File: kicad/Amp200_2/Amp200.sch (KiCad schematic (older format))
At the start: 38 parts, among them J1 Conn, J10 Conn, J2 Conn, J3 Conn, J5 Conn, J6 Conn, J7 Conn, J8 Conn, J9 Conn, U2 NCP1117-3.3

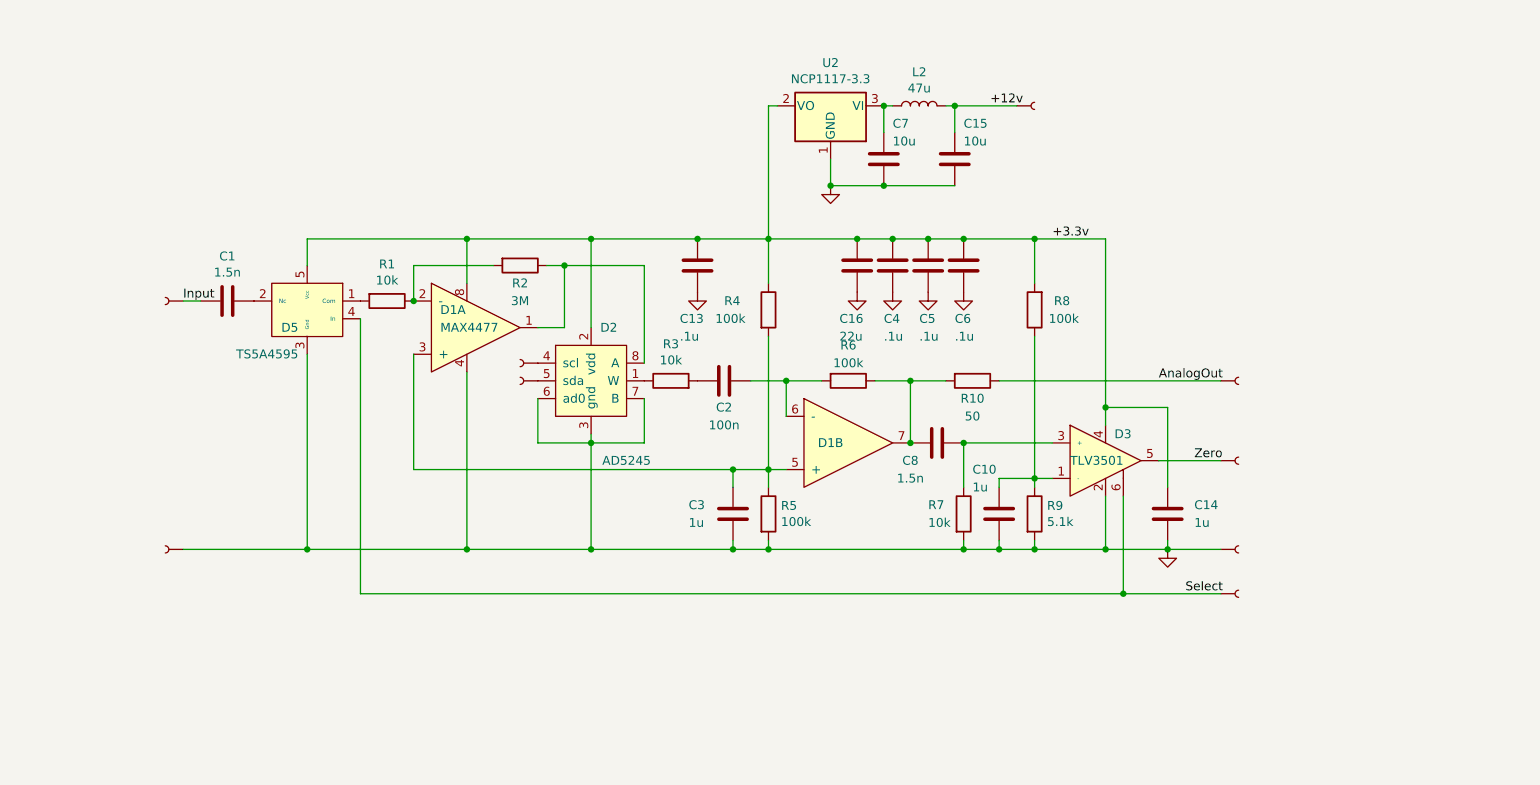
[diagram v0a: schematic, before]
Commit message: изменено:      kicad/Amp200_2/Amp200-cache.lib 	изменено:      kicad/Amp200_2/Amp200.kicad_pcb 	изменено:      kicad/Amp200_2/Amp200.kicad_pcb-bak 	изменено:      kicad/Amp200_2/Amp200.sch 	изменено:      kicad/Amp200_2/Amp200.sch-bak 	изменено:      kicad/Amp200_2/fp-info-cache 	изменено:      kicad/Anemometr_200_F303/fp-info-cache 	изменено:      stm32cubeide/Anemometer/Release/makefile 	изменено:      stm32cubeide/Anemometer_200_F303/Anemometer_200_F303.ioc 	изменено:      stm32cubeide/Anemometer_200_F303/Core/Inc/main.h 	изменено:      stm32cubeide/Anemometer_200_F303/Core/Inc/stm32f3xx_it.h 	изменено:      stm32cubeide/Anemometer_200_F303/Core/Src/main.c 	изменено:      stm32cubeide/Anemometer_200_F303/Core/Src/stm32f3xx_hal_msp.c 	изменено:      stm32cubeide/Anemometer_200_F303/Core/Src/stm32f3xx_it.c 	изменено:      stm32cubeide/Anemometer_200_F303/Debug/Anemometer_200_F303.bin 	изменено:      stm32cubeide/Anemometer_200_F303/Debug/Anemometer_200_F303.elf 	изменено:      stm32cubeide/Anemometer_200_F303/Debug/Anemometer_200_F303.list 	изменено:      stm32cubeide/Anemometer_200_F303/Debug/Anemometer_200_F303.map 	изменено:      stm32cubeide/Anemometer_200_F303/Debug/Core/Src/main.o 	изменено:      stm32cubeide/Anemometer_200_F303/Debug/Core/Src/main.su 	изменено:      stm32cubeide/Anemometer_200_F303/Debug/Core/Src/stm32f3xx_hal_msp.o 	изменено:      stm32cubeide/Anemometer_200_F303/Debug/Core/Src/stm32f3xx_hal_msp.su 	изменено:      stm32cubeide/Anemometer_200_F303/Debug/Core/Src/stm32f3xx_it.o 	изменено:      stm32cubeide/Anemometer_200_F303/Debug/Core/Src/stm32f3xx_it.su
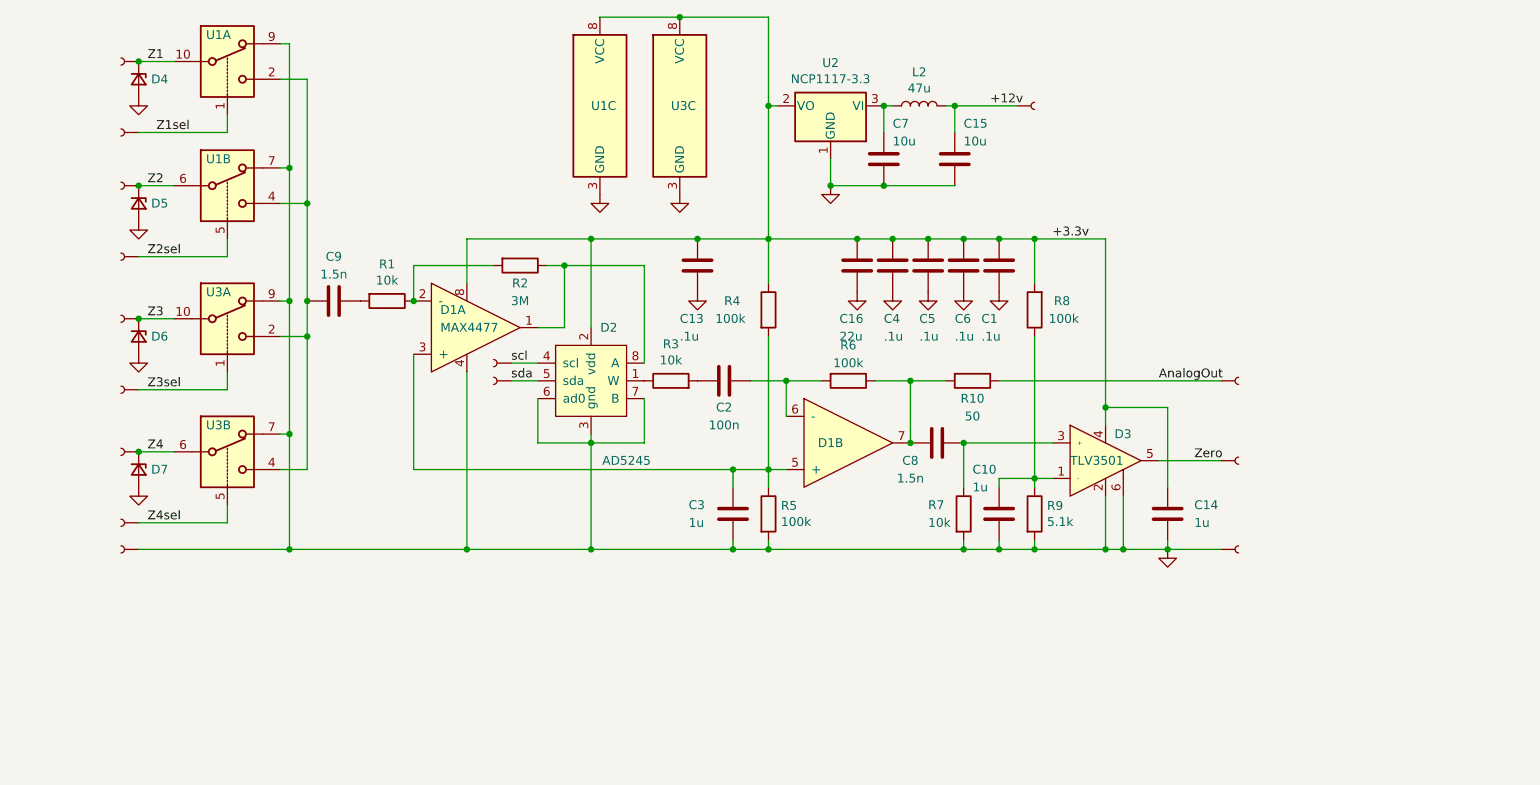
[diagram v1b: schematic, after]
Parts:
- removed D5: TS5A4595, Package_TO_SOT_SMD:SOT-23-5, symbol Amp200-rescue:TS5A4595-My_Library
- added C9: 1.5n, Capacitor_SMD:C_0603_1608Metric, symbol Device:C
- added D4, D5, D6, D7: BZ55C2V7, Diode_SMD:D_MiniMELF, symbol Device:D_Zener_Small
- added J11, J12, J13, J14, J15, J16: Conn, My-library:SMD-CONN, symbol Amp200-rescue:Conn-My_Library
- added U1, U3: TS5A23159DGS, Package_SO:VSSOP-10_3x3mm_P0.5mm, symbol Analog_Switch:TS5A23159DGS
- C1: value 1.5n -> .1u; footprint Capacitor_SMD:C_0603_1608Metric -> Capacitor_SMD:C_0805_2012Metric
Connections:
- net +3.3v: now also C1.1, U1.8 (VCC), U3.8 (VCC)
- net GND: now also C1.2, D3.6, D4.2 (A), D5.2 (A), D6.2 (A), D7.2 (A), U1.3 (GND), U1.7, U1.9, U3.3 (GND), U3.7, U3.9
- net at R1.2: now also C9.1
- net scl: now reaches D2.4 (scl), J2.1
- net sda: now reaches D2.5 (sda), J3.1
- net Input renamed Z1
- net Z1: now also D4.1 (K), U1.10; no longer C1.2
- net Select renamed Z1sel
- net Z1sel: now also U1.1; no longer D3.6
- new net: C9.2, U1.2, U1.4, U3.2, U3.4
- new net Z2: D5.1 (K), J11.1, U1.6
- new net Z2sel: J12.1, U1.5
- new net Z3: D6.1 (K), J13.1, U3.10
- new net Z3sel: J14.1, U3.1
- new net Z4: D7.1 (K), J15.1, U3.6
- new net Z4sel: J16.1, U3.5

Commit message: изменено:      kicad/Amp200_2/Amp200-cache.lib 	изменено:      kicad/Amp200_2/Amp200.kicad_pcb 	изменено:      kicad/Amp200_2/Amp200.kicad_pcb-bak 	изменено:      kicad/Amp200_2/Amp200.sch 	изменено:      kicad/Amp200_2/Amp200.sch-bak 	изменено:      kicad/Amp200_2/fp-info-cache 	изменено:      kicad/Anemometr_200_F303/Anemometr_200_F303.kicad_pcb 	изменено:      kicad/Anemometr_200_F303/Anemometr_200_F303.kicad_pcb-bak 	изменено:      kicad/Anemometr_200_F303/Anemometr_200_F303.sch 	изменено:      kicad/Anemometr_200_F303/Anemometr_200_F303.sch-bak 	изменено:      stm32cubeide/Anemometer_200_F303/.cproject 	изменено:      stm32cubeide/Anemometer_200_F303/.mxproject 	изменено:      stm32cubeide/Anemometer_200_F303/.settings/language.settings.xml 	изменено:      stm32cubeide/Anemometer_200_F303/.settings/stm32cubeide.project.prefs 	изменено:      stm32cubeide/Anemometer_200_F303/Anemometer_200_F303.ioc 	изменено:      stm32cubeide/Anemometer_200_F303/Anemometer_200_F303.launch 	изменено:      stm32cubeide/Anemometer_200_F303/Core/Inc/main.h 	изменено:      stm32cubeide/Anemometer_200_F303/Core/Inc/stm32f3xx_hal_conf.h 	изменено:      stm32cubeide/Anemometer_200_F303/Core/Inc/stm32f3xx_it.h 	изменено:      stm32cubeide/Anemometer_200_F303/Core/Src/main.c 	изменено:      stm32cubeide/Anemometer_200_F303/Core/Src/stm32f3xx_hal_msp.c 	изменено:      stm32cubeide/Anemometer_200_F303/Core/Src/stm32f3xx_it.c 	удалено:       stm32cubeide/Anemometer_200_F303/Debug/Anemometer_200_F303.bin 	изменено:      stm32cubeide/Anemometer_200_F303/Debug/Anemometer_200_F303.elf 	изменено:      stm32cubeide/Anemometer_200_F303/Debug/Anemometer_200_F303.list 	изменено:      stm32cubeide/Anemometer_200_F303/Debug/Anemometer_200_F303.map 	изменено:      stm32cubeide/Anemometer_200_F303/Debug/Core/Src/main.d 	изменено:      stm32cubeide/Anemometer_200_F303/Debug/Core/Src/main.o 	изменено:      stm32cubeide/Anemometer_200_F303/Debug/Core/Src/main.su 	изменено:      stm32cubeide/Anemometer_200_F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
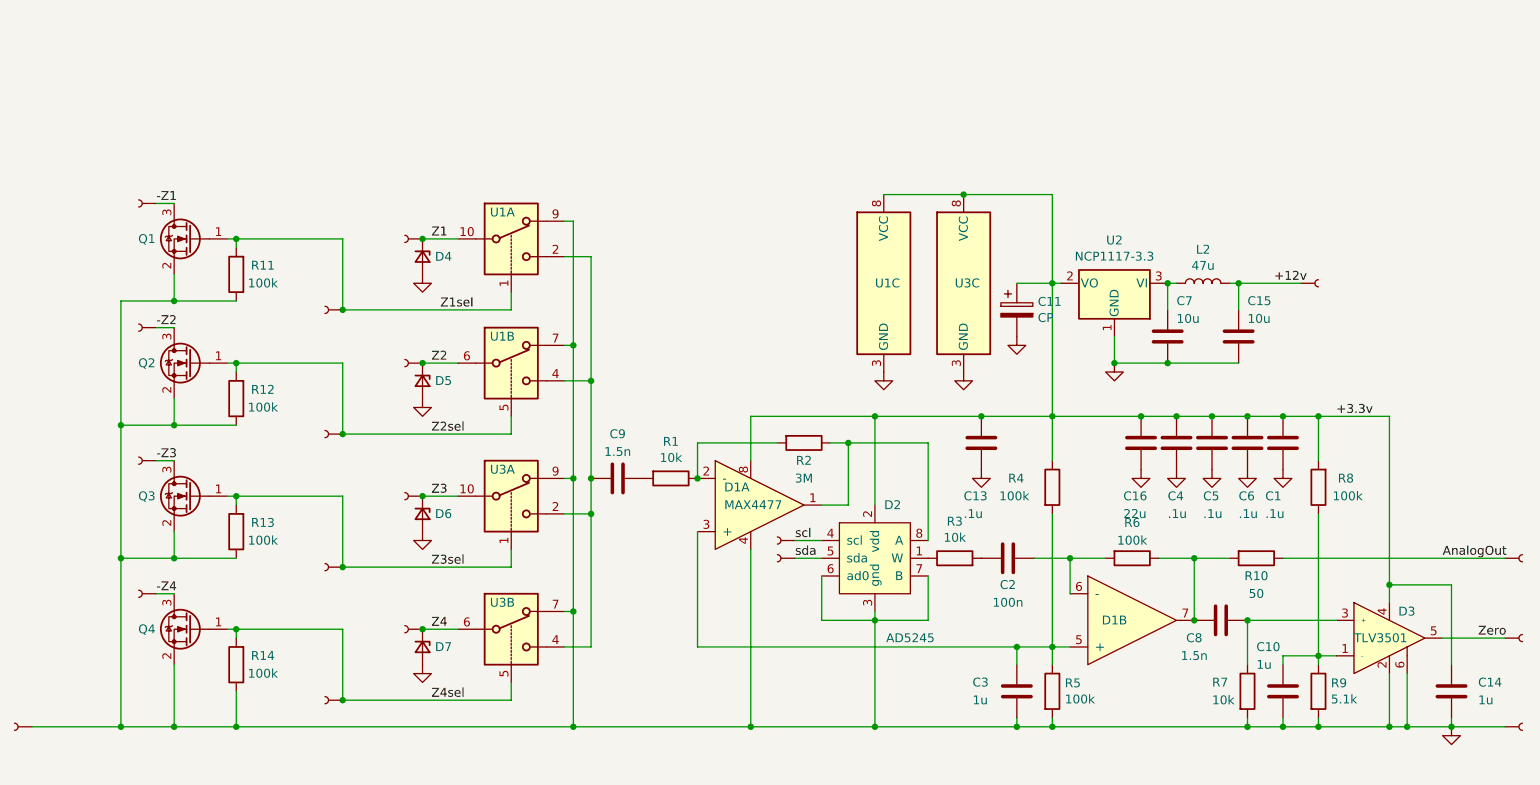
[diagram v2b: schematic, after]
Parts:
- added C11: CP, Capacitor_Tantalum_SMD:CP_EIA-6032-28_Kemet-C, symbol Device:CP
- added J17, J18, J19, J4: Conn, My-library:SMD-CONN, symbol Amp200-rescue:Conn-My_Library
- added Q1, Q2, Q3, Q4: Q_NMOS_GSD, Package_TO_SOT_SMD:SOT-23, symbol Device:Q_NMOS_GSD
- added R11, R12, R13, R14: 100k, Resistor_SMD:R_0603_1608Metric, symbol Device:R
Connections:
- net +3.3v: now also C11.1
- net GND: now also C11.2, Q1.2 (S), Q2.2 (S), Q3.2 (S), Q4.2 (S), R11.1, R12.1, R13.1, R14.1
- net Z1sel: now also Q1.1 (G), R11.2
- net Z2sel: now also Q2.1 (G), R12.2
- net Z3sel: now also J19.1, Q3.1 (G), R13.2; no longer J14.1
- net Z4sel: now also Q4.1 (G), R14.2
- new net -Z1: J4.1, Q1.3 (D)
- new net -Z2: J17.1, Q2.3 (D)
- new net -Z3: J14.1, Q3.3 (D)
- new net -Z4: J18.1, Q4.3 (D)
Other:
- moved on the sheet: C1, C10, C13, C14, C15, C16, C2, C3, C4, C5, C6, C7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

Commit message: изменено:      kicad/Amp200_2/Amp200-cache.lib 	изменено:      kicad/Amp200_2/Amp200.kicad_pcb 	изменено:      kicad/Amp200_2/Amp200.kicad_pcb-bak 	изменено:      kicad/Amp200_2/Amp200.sch 	изменено:      kicad/Amp200_2/Amp200.sch-bak
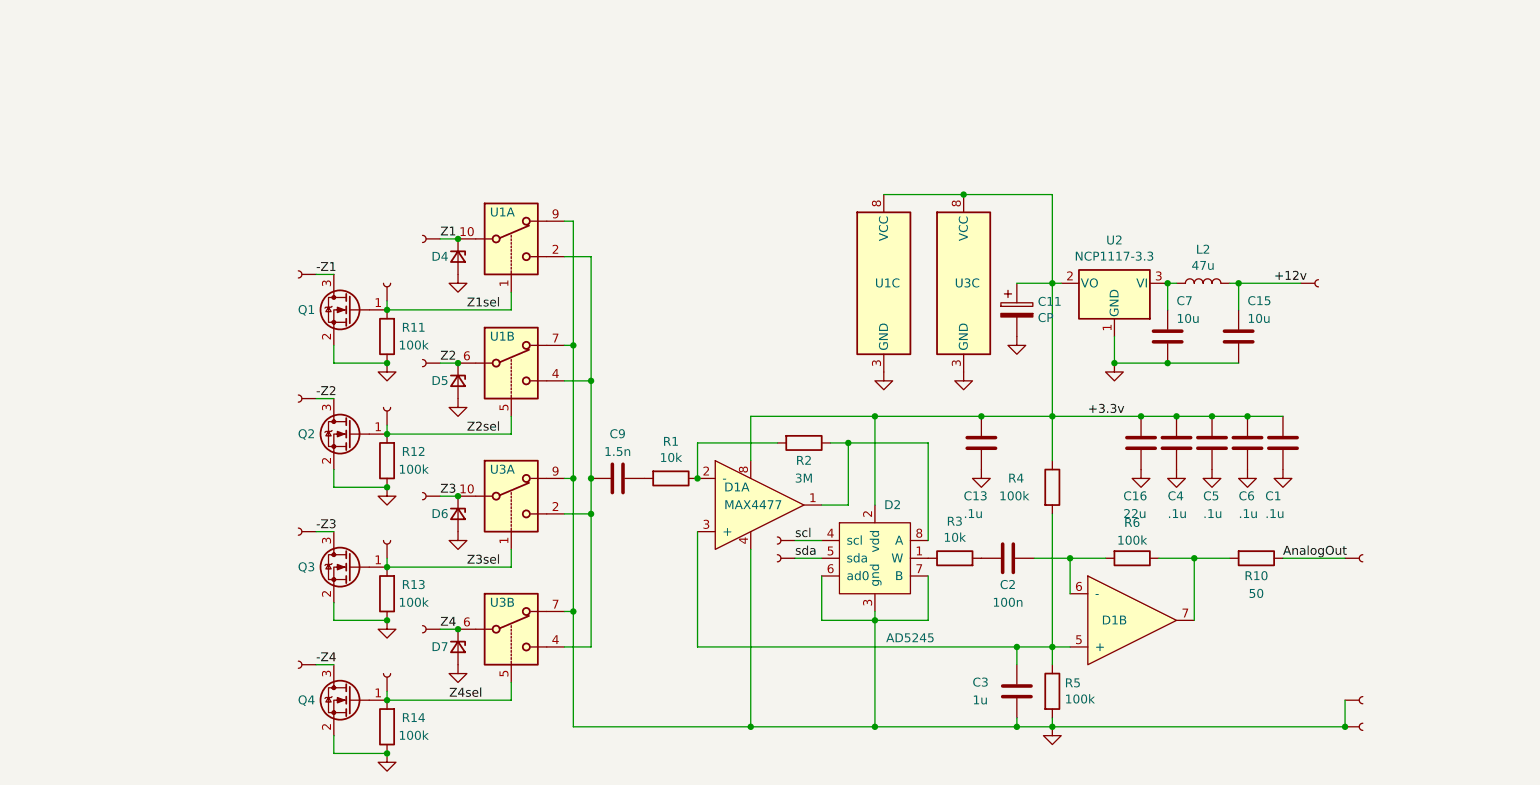
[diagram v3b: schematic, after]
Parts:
- removed C10: 1u, Capacitor_SMD:C_0603_1608Metric, symbol Device:C
- removed C14: 1u, Capacitor_SMD:C_0805_2012Metric, symbol Device:C
- removed C8: 1.5n, Capacitor_SMD:C_0603_1608Metric, symbol Device:C
- removed D3: TLV3501, Package_TO_SOT_SMD:SOT-23-6, symbol Amp200-rescue:TLV3501-2-My_Library
- removed J6: Conn, My-library:SMD-CONN, symbol Amp200-rescue:Conn-My_Library
- removed R7: 10k, Resistor_SMD:R_0603_1608Metric, symbol Device:R
- removed R8: 100k, Resistor_SMD:R_0603_1608Metric, symbol Device:R
- removed R9: 5.1k, Resistor_SMD:R_0603_1608Metric, symbol Device:R
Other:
- moved on the sheet: D4, D5, D6, D7, Q1, Q2, Q3, Q4, R11, R12, R13, R14

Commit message: изменено:      kicad/Amp200_2/Amp200-cache.lib 	изменено:      kicad/Amp200_2/Amp200-rescue.lib 	изменено:      kicad/Amp200_2/Amp200.kicad_pcb 	изменено:      kicad/Amp200_2/Amp200.kicad_pcb-bak 	изменено:      kicad/Amp200_2/Amp200.sch 	изменено:      kicad/Amp200_2/Amp200.sch-bak 	изменено:      kicad/Amp200_2/sym-lib-table 	изменено:      kicad/Anemometer_200_G473/Anemometer_200_G473-cache.lib 	изменено:      kicad/Anemometer_200_G473/Anemometer_200_G473.sch 	изменено:      kicad/Anemometer_200_G473/Anemometer_200_G473.sch-bak 	изменено:      kicad/Anemometer_200_G473/sym-lib-table
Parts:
- added C8: 470u, Capacitor_Tantalum_SMD:CP_EIA-6032-28_Kemet-C, symbol Device:CP
- C11: value CP -> 1000u
- D2: symbol My_Library:AD5245 -> Amp200-rescue:AD5245-My_Library
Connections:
- net GND: now also C8.2
- net at C7.1, L2.1, U2.3 (VI): now also C8.1
- net +12v renamed +5v
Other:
- moved on the sheet: C1, C13, C15, C16, C4, C5, C6, L2, R10, R2
